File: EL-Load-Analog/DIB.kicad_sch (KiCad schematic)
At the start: 7 parts, among them J3 Conn_02x06_Odd_Even, U5 24LC32, X3 DIB Pheriperal connector

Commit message: Added snubber on input, bananajacks, sense connector, some cleanup.
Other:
- title: (none) -> Electronic Load Analog Test Board
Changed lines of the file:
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@@
 (kicad_sch (version 20230121) (generator eeschema)
   (paper "A4")
+  (title_block
+    (title "Electronic Load Analog Test Board")
+    (date "2023-12-30")
+    (rev "${VERSION}")
+    (comment 1 "License: CERN-OHL-W-2.0")
+  )
   (junction (at 32.385 44.45) (diameter 0) (color 0 0 0 0)
   )

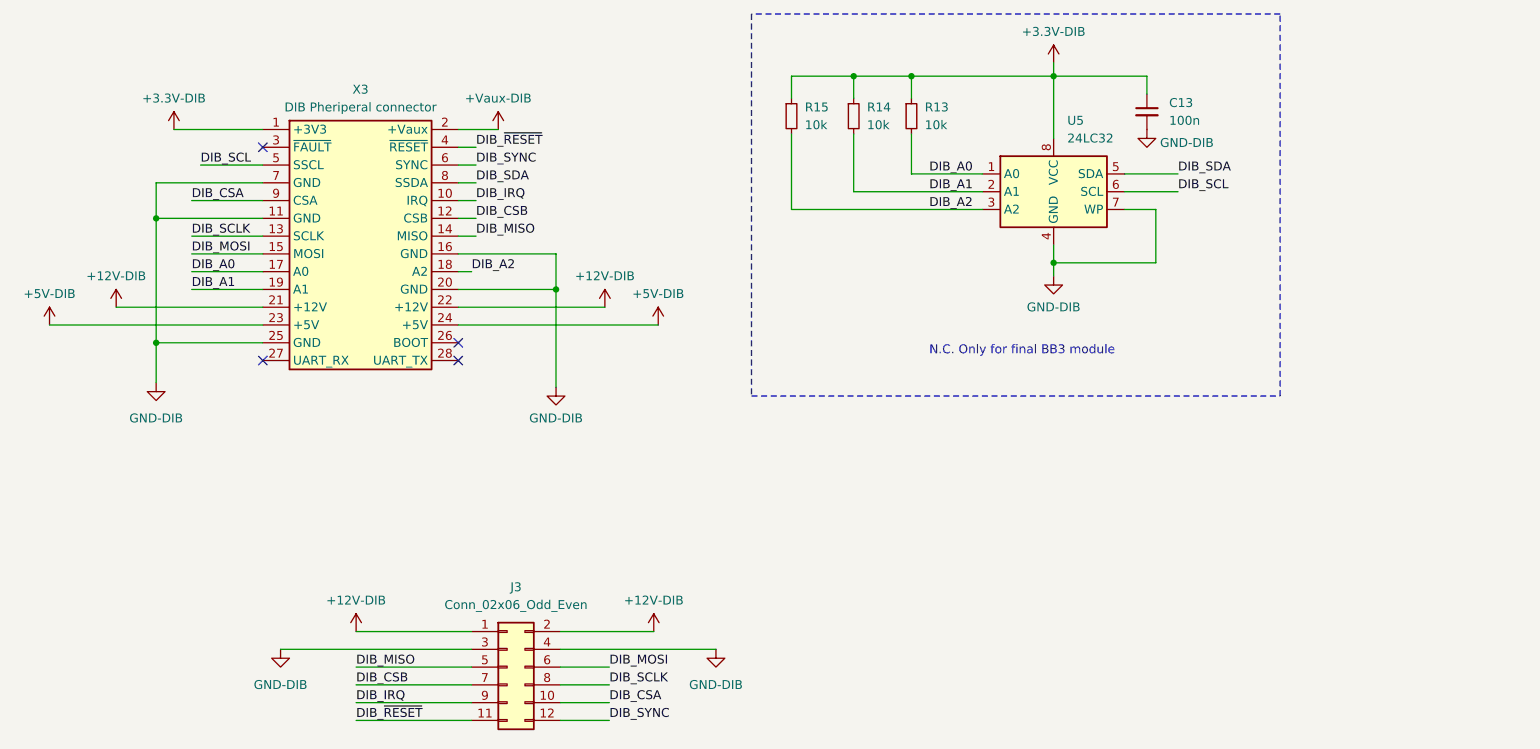
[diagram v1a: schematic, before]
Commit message: Added SenseError detection (including ocmponents), added clearances, fixed few BOM items.
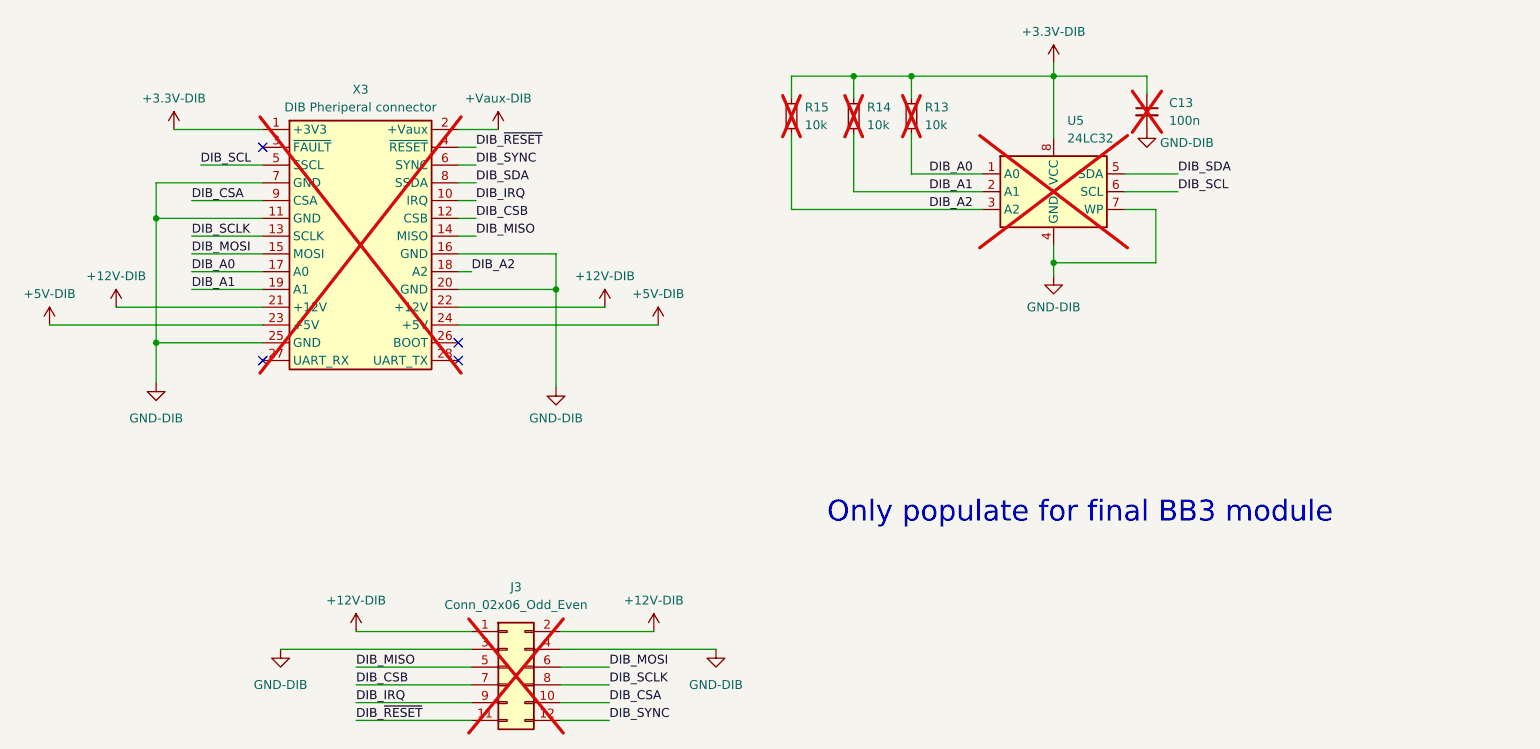
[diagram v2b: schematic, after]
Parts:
- C13: Part Name (none) -> C_100.0nF_0805_20%; now not fitted; now left out of the parts list
- J3: Part Name (none) -> H_Female_2x6_SMD; now not fitted; now left out of the parts list
- R13, R14, R15: Part Name (none) -> R_10.0kΩ_0805_1%; now not fitted; now left out of the parts list
- U5: Part Name (none) -> U_24C64; now not fitted; now left out of the parts list
- X3: now not fitted; now left out of the parts list
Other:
- note added: "Only populate for final BB3 module"
- note removed: "N.C. Only for final BB3 module"
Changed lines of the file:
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@@
     (stroke (width 0) (type default))
-  )
-  (polyline (pts (xy 117.475 15.24) (xy 117.475 69.85))
-    (stroke (width 0) (type dash))
   )
   (wire (pts (xy 150.495 40.64) (xy 132.08 40.64))
@@
     (stroke (width 0) (type default))
   )
-  (polyline (pts (xy 193.04 69.85) (xy 193.04 15.24))
-    (stroke (width 0) (type dash))
-  )
   (wire (pts (xy 38.735 36.83) (xy 47.625 36.83))
     (stroke (width 0) (type default))
@@
     (stroke (width 0) (type default))
   )
-  (polyline (pts (xy 117.475 69.85) (xy 193.04 69.85))
-    (stroke (width 0) (type dash))
-  )
   (wire (pts (xy 75.565 31.75) (xy 81.28 31.75))
     (stroke (width 0) (type default))
   )
-  (polyline (pts (xy 193.04 15.24) (xy 117.475 15.24))
-    (stroke (width 0) (type dash))
-  )
   (wire (pts (xy 37.465 52.07) (xy 47.625 52.07))
     (stroke (width 0) (type default))
   )
-  (text "N.C. Only for final BB3 module" (at 142.875 64.135 0)
-    (effects (font (size 1.27 1.27)) (justify left bottom))
+  (text "Only populate for final BB3 module" (at 128.27 88.265 0)
+    (effects (font (size 3 3)) (justify left bottom))
   )
   (label "DIB_CSB" (at 60.96 111.125 0) (fields_autoplaced)
@@
   )
   (symbol (lib_id "Device:R_Small") (at 132.08 29.845 0) (unit 1)
-    (in_bom yes) (on_board yes) (dnp no) (fields_autoplaced)
+    (in_bom no) (on_board yes) (dnp yes) (fields_autoplaced)
     (property "Reference" "R14" (at 133.985 28.575 0)
       (effects (font (size 1.27 1.27)) (justify left))
@@
       (effects (font (size 1.27 1.27)) hide)
     )
+    (property "Part Name" "R_10.0kΩ_0805_1%" (at 132.08 29.845 0)
+      (effects (font (size 1.27 1.27)) hide)
+    )
     (pin "1")
     (pin "2")
@@
   )
   (symbol (lib_id "Connector_Generic:Conn_02x06_Odd_Even") (at 82.55 108.585 0) (unit 1)
-    (in_bom yes) (on_board yes) (dnp no) (fields_autoplaced)
+    (in_bom no) (on_board yes) (dnp yes) (fields_autoplaced)
     (property "Reference" "J3" (at 83.82 97.155 0)
       (effects (font (size 1.27 1.27)))
@@
     )
     (property "Datasheet" "~" (at 82.55 108.585 0)
+      (effects (font (size 1.27 1.27)) hide)
+    )
+    (property "Part Name" "H_Female_2x6_SMD " (at 82.55 108.585 0)
       (effects (font (size 1.27 1.27)) hide)
     )
@@
   )
   (symbol (lib_id "EEZ-DIB:DIB_Peripheral") (at 47.625 31.75 0) (unit 1)
-    (in_bom yes) (on_board yes) (dnp no) (fields_autoplaced)
+    (in_bom no) (on_board yes) (dnp yes) (fields_autoplaced)
     (property "Reference" "X3" (at 61.595 26.035 0)
       (effects (font (size 1.27 1.27)))
@@
   )
   (symbol (lib_id "Device:C_Small") (at 173.99 29.21 0) (unit 1)
-    (in_bom yes) (on_board yes) (dnp no) (fields_autoplaced)
+    (in_bom no) (on_board yes) (dnp yes) (fields_autoplaced)
     (property "Reference" "C13" (at 177.165 27.9463 0)
       (effects (font (size 1.27 1.27)) (justify left))
@@
       (effects (font (size 1.27 1.27)) hide)
     )
+    (property "Part Name" "C_100.0nF_0805_20%" (at 173.99 29.21 0)
+      (effects (font (size 1.27 1.27)) hide)
+    )
     (pin "1")
     (pin "2")
@@
   )
   (symbol (lib_id "Memory_EEPROM:24LC32") (at 160.655 40.64 0) (unit 1)
-    (in_bom yes) (on_board yes) (dnp no) (fields_autoplaced)
+    (in_bom no) (on_board yes) (dnp yes) (fields_autoplaced)
     (property "Reference" "U5" (at 162.6109 30.48 0)
       (effects (font (size 1.27 1.27)) (justify left))
@@
     )
     (property "Datasheet" "http://ww1.microchip.com/downloads/en/DeviceDoc/21072G.pdf" (at 160.655 40.64 0)
+      (effects (font (size 1.27 1.27)) hide)
+    )
+    (property "Part Name" "U_24C64 " (at 160.655 40.64 0)
       (effects (font (size 1.27 1.27)) hide)
     )
@@
   )
   (symbol (lib_id "Device:R_Small") (at 123.19 29.845 0) (unit 1)
-    (in_bom yes) (on_board yes) (dnp no) (fields_autoplaced)
+    (in_bom no) (on_board yes) (dnp yes) (fields_autoplaced)
     (property "Reference" "R15" (at 125.095 28.575 0)
       (effects (font (size 1.27 1.27)) (justify left))
@@
     )
     (property "Datasheet" "~" (at 123.19 29.845 0)
+      (effects (font (size 1.27 1.27)) hide)
+    )
+    (property "Part Name" "R_10.0kΩ_0805_1%" (at 123.19 29.845 0)
       (effects (font (size 1.27 1.27)) hide)
     )
@@
   )
   (symbol (lib_id "Device:R_Small") (at 140.335 29.845 0) (unit 1)
-    (in_bom yes) (on_board yes) (dnp no) (fields_autoplaced)
+    (in_bom no) (on_board yes) (dnp yes) (fields_autoplaced)
     (property "Reference" "R13" (at 142.24 28.575 0)
       (effects (font (size 1.27 1.27)) (justify left))
@@
       (effects (font (size 1.27 1.27)) hide)
     )
+    (property "Part Name" "R_10.0kΩ_0805_1%" (at 140.335 29.845 0)
+      (effects (font (size 1.27 1.27)) hide)
+    )
